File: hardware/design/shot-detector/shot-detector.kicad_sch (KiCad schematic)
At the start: 7 parts

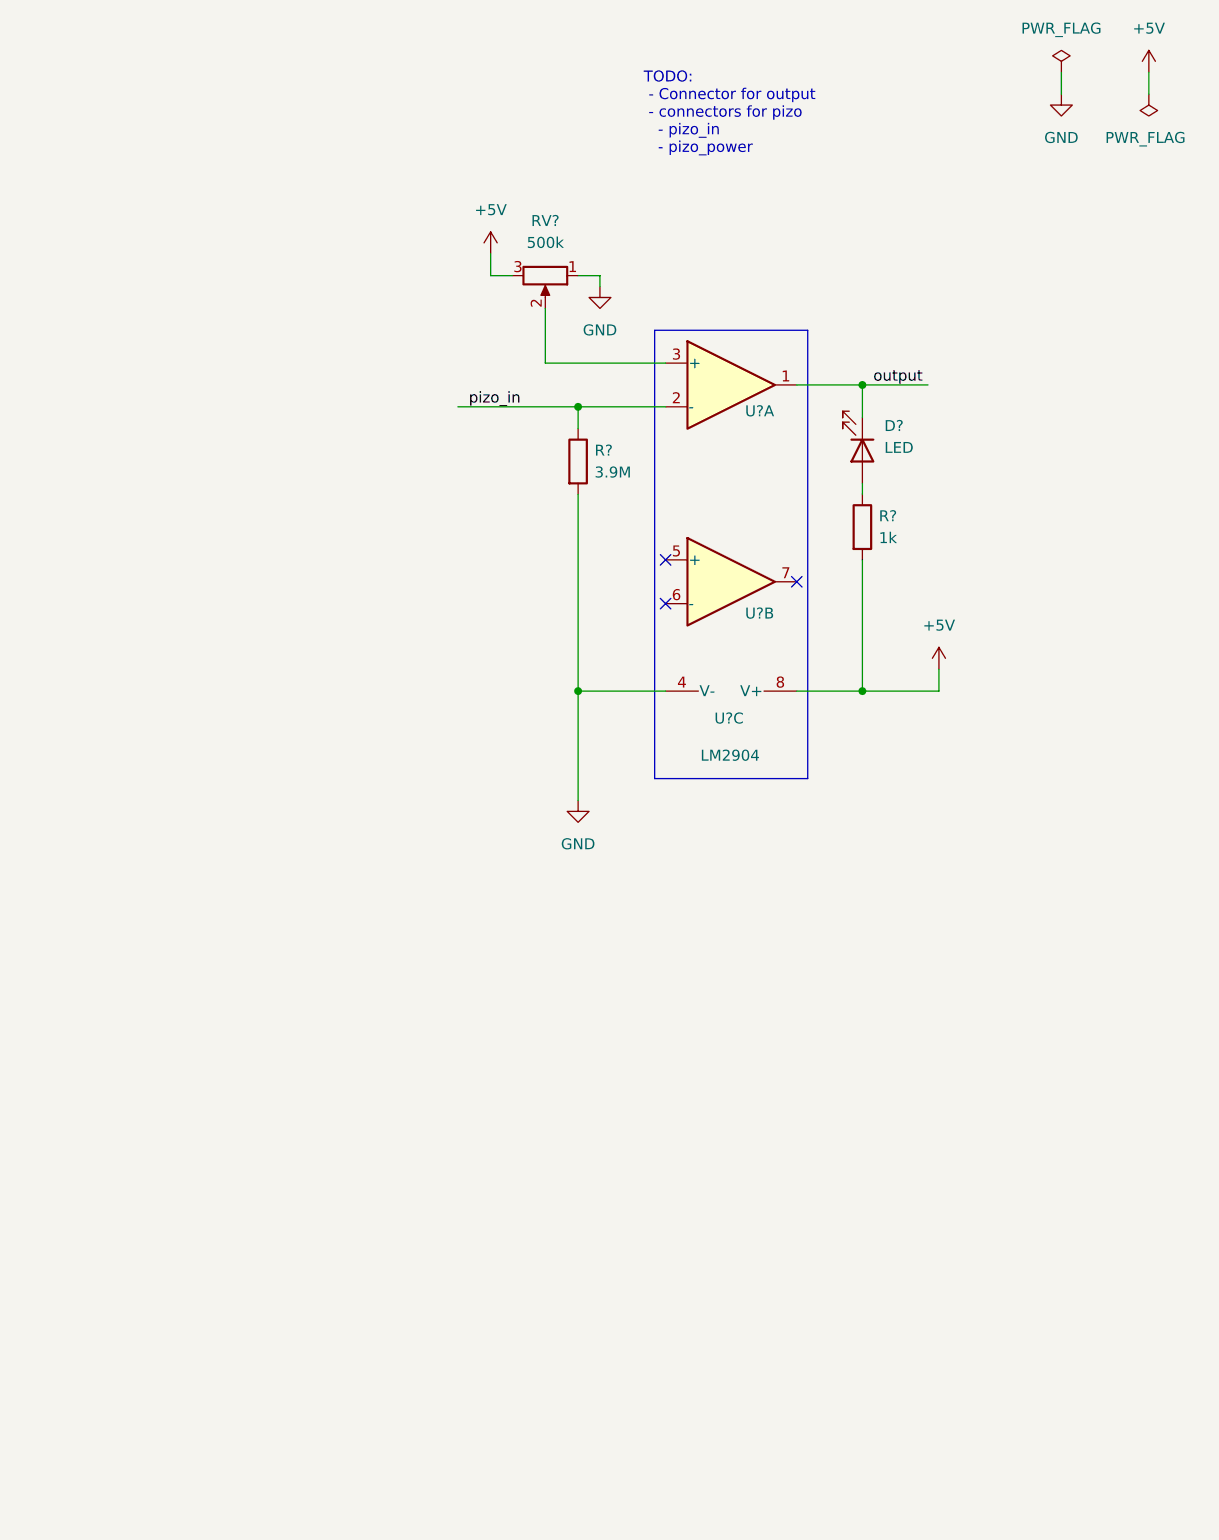
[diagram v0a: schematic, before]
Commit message: Updating schematic to use the LM393 along with some related docs
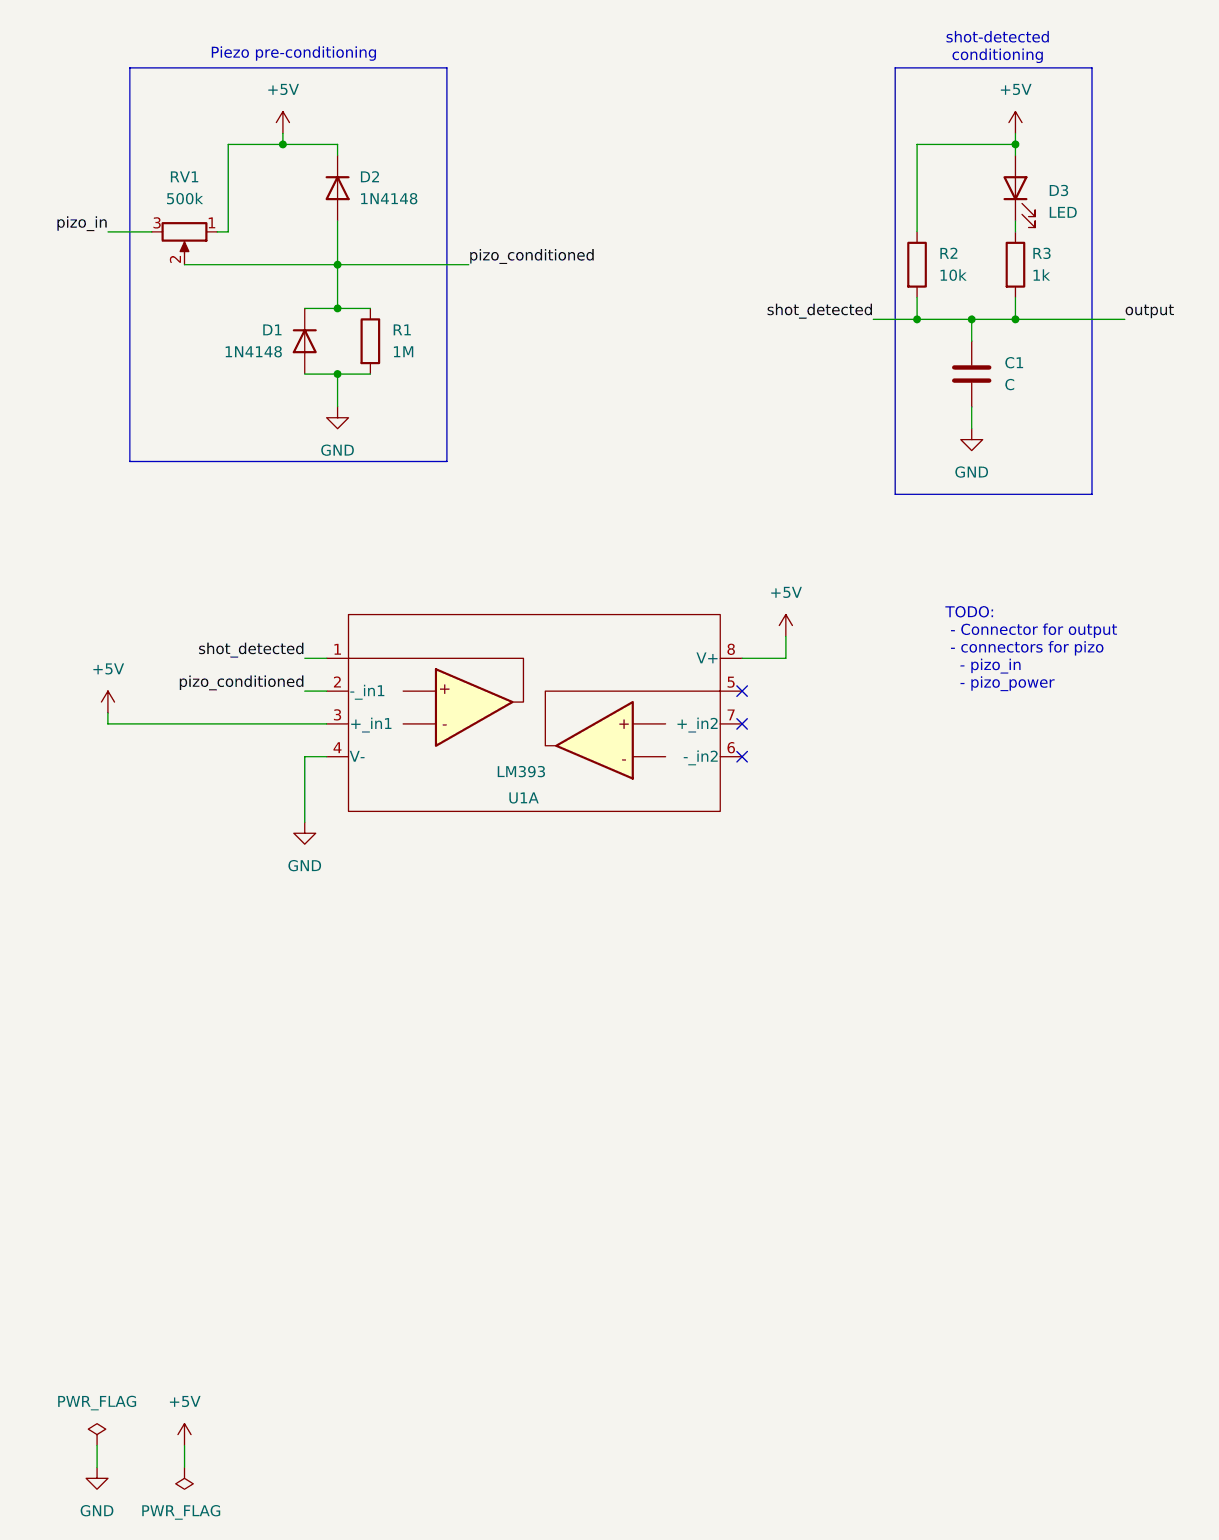
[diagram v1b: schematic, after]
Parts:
- removed D?: LED, symbol Device:LED
- removed R?: 3.9M, symbol Device:R
- removed R?: 1k, symbol Device:R
- removed RV?: 500k, symbol Device:R_Potentiometer
- removed U? (x2): LM2904, symbol Amplifier_Operational:LM2904
- removed U?: LM2904, Package_SO:SO-8_3.9x4.9mm_P1.27mm, symbol Amplifier_Operational:LM2904
- added C1: C, symbol Device:C
- added D1, D2: 1N4148, Diode_THT:D_DO-35_SOD27_P7.62mm_Horizontal, symbol Diode:1N4148
- added D3: LED, symbol Device:LED
- added R1: 1M, symbol Device:R
- added R2: 10k, symbol Device:R
- added R3: 1k, symbol Device:R
- added RV1: 500k, symbol Device:R_Potentiometer
- added U1: LM393, symbol Comparator:LM393
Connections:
- net +5V: now also D2.1 (K), D3.2 (A), R2.1, RV1.1, U1.3 (+_in1), U1.8 (V+)
- net GND: now also C1.2, D1.2 (A), R1.2, U1.4 (V-)
- net output: now also C1.1, R2.2, R3.2, U1.1
- net pizo_in: now also RV1.3
- new net: D3.1 (K), R3.1
- new net pizo_conditioned: D1.1 (K), D2.2 (A), R1.1, RV1.2, U1.2 (-_in1)
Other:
- note added: "Piezo pre-conditioning"
- note added: "shot-detected conditioning"

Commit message: Progress on schematic and PCB.
Finished getting all the parts placed, and most all footprints.
Getting the general layout started on PCB.
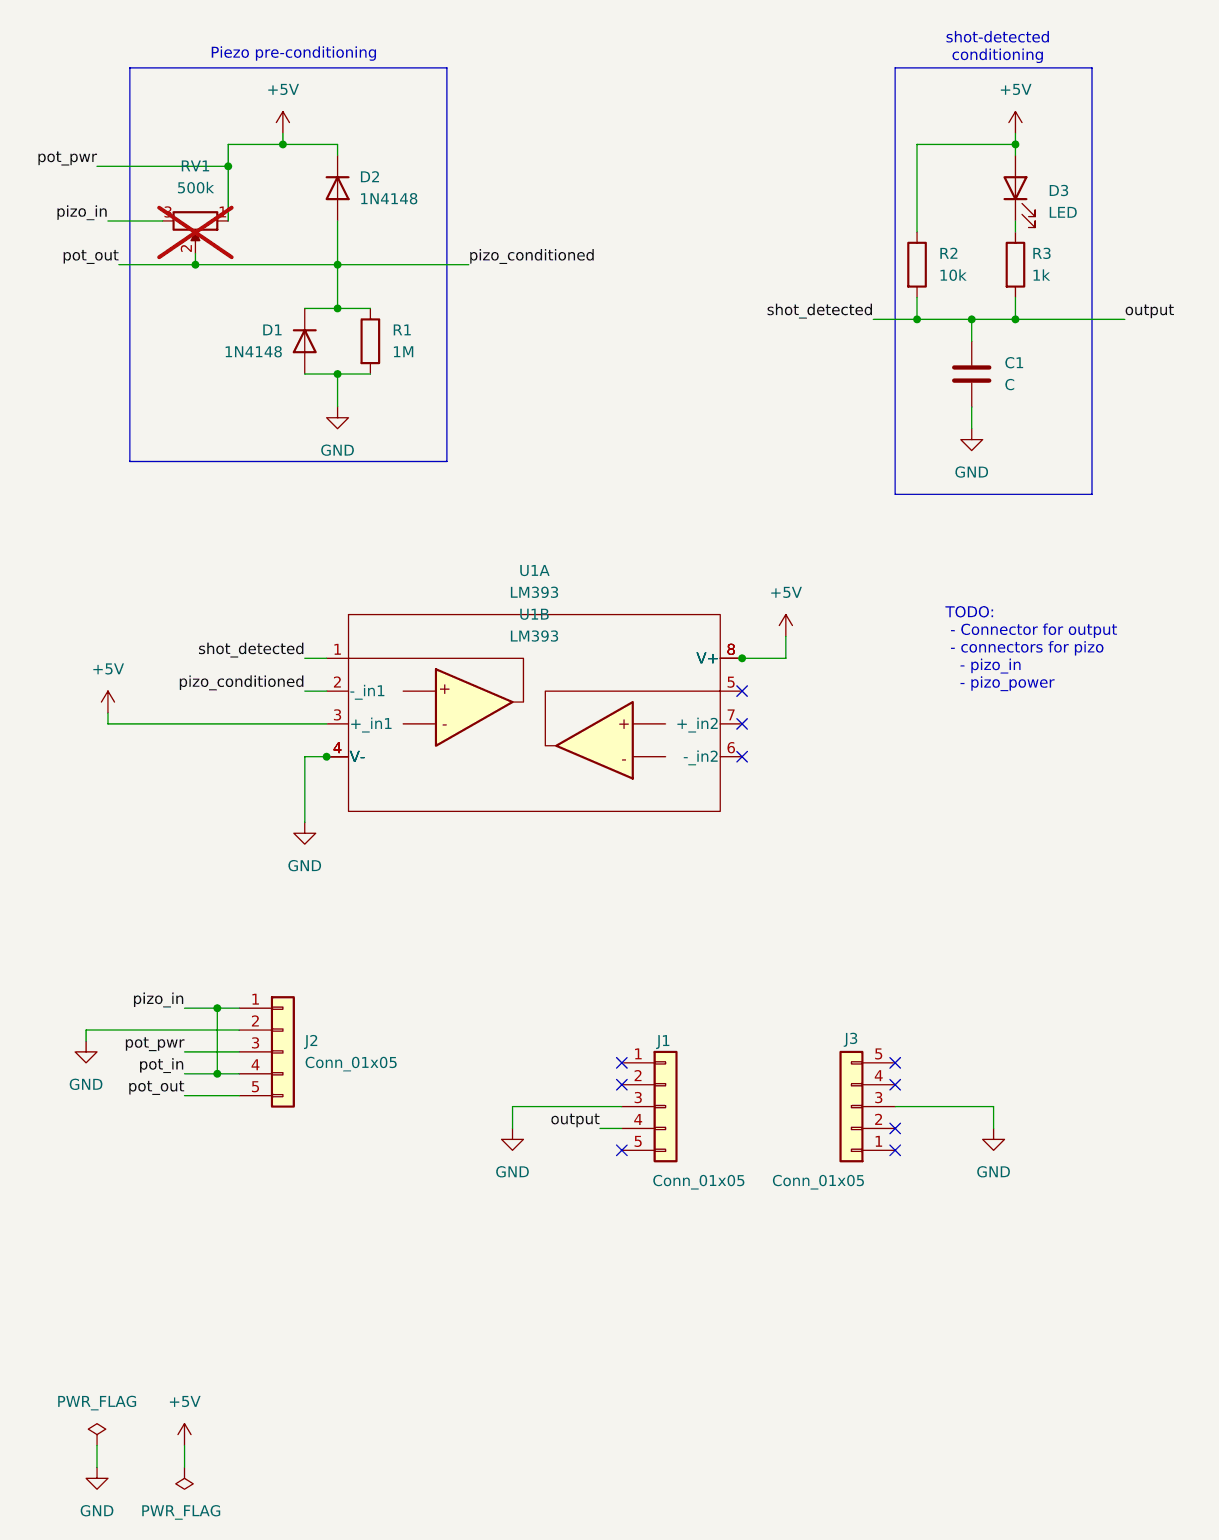
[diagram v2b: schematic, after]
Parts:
- removed U1: LM393, symbol Comparator:LM393
- added J1, J3: Conn_01x05, Connector_PinHeader_2.54mm:PinHeader_1x05_P2.54mm_Vertical, symbol Connector_Generic:Conn_01x05
- added J2: Conn_01x05, custom-project-lib:1x05_smt_wire_solder, symbol Connector_Generic:Conn_01x05
- added U1: LM393, Package_SO:TSSOP-8_3x3mm_P0.65mm, symbol lm393-custom:LM393
- C1: footprint (none) -> Capacitor_SMD:C_1206_3216Metric
- D1, D2: footprint Diode_THT:D_DO-35_SOD27_P7.62mm_Horizontal -> Diode_SMD:D_SOD-123
- D3: footprint (none) -> LED_SMD:LED_1206_3216Metric
- R1, R2, R3: footprint (none) -> Resistor_SMD:R_1206_3216Metric
- RV1: now not fitted
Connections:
- net +5V: now also J2.3 (Pin_3), U1.3 (+_in1), U1.8 (V+), U1.8 (V+)
- net GND: now also J1.3 (Pin_3), J2.2 (Pin_2), J3.3 (Pin_3), U1.4 (V-), U1.4 (V-)
- net output: now also J1.4 (Pin_4), U1.1
- net pizo_conditioned: now also J2.5 (Pin_5), U1.2 (-_in1)
- net pizo_in: now also J2.1 (Pin_1), J2.4 (Pin_4)
- no-connect marks 3 -> 10
